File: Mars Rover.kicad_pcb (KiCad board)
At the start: 2 copper layers, 39 parts, among them U1401 PCA9685PW, U1402 ADS7828, U202 L298HN, U402 L298HN, U502 L298HN

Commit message: on to pcbs
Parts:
- added C101: 22uF, Capacitor_SMD:C_0805_2012Metric, F.Cu at (54.1, 139.1)
- added C102: 0.1uF, Capacitor_SMD:C_0805_2012Metric, F.Cu at (61.0, 137.3)
- added C1401: C, Capacitor_SMD:C_0805_2012Metric, F.Cu at (119.9, 21.3)
- added C201: 100nF, Capacitor_SMD:C_0805_2012Metric, F.Cu at (198.3, 53.4)
- added C202: 100nF, Capacitor_SMD:C_0805_2012Metric, F.Cu at (201.7, 53.4)
- added C203: 100nF, Capacitor_SMD:C_0805_2012Metric, F.Cu at (205.1, 53.4)
- added C401: 100nF, Capacitor_SMD:C_0805_2012Metric, F.Cu at (130.5, 118.3)
- added C402: 100nF, Capacitor_SMD:C_0805_2012Metric, F.Cu at (133.9, 118.3)
- added C403: 100nF, Capacitor_SMD:C_0805_2012Metric, F.Cu at (137.3, 118.3)
- added C501: 100nF, Capacitor_SMD:C_0805_2012Metric, F.Cu at (112.9, 127.2)
- added C502: 100nF, Capacitor_SMD:C_0805_2012Metric, F.Cu at (116.3, 127.2)
- added C503: 100nF, Capacitor_SMD:C_0805_2012Metric, F.Cu at (119.7, 127.2)
- added C601: 0.1uF, Capacitor_SMD:C_0805_2012Metric, F.Cu at (211.3, 25.3)
- added C602: 0.1uF, Capacitor_SMD:C_0805_2012Metric, F.Cu at (214.7, 23.3)
- added C603: 1nF, Capacitor_SMD:C_0805_2012Metric, F.Cu at (218.2, 21.3)
- added C604: 1uF, Capacitor_SMD:C_0805_2012Metric, F.Cu at (211.3, 27.2)
- added C605: 0.1uF, Capacitor_SMD:C_0805_2012Metric, F.Cu at (208.6, 31.2)
- added C606: 0.1uF, Capacitor_SMD:C_0805_2012Metric, F.Cu at (214.7, 27.2)
- added C607: 1nF, Capacitor_SMD:C_0805_2012Metric, F.Cu at (218.1, 23.2)
- added C608: 1nF, Capacitor_SMD:C_0805_2012Metric, F.Cu at (214.7, 25.3)
- added C609: C, Capacitor_SMD:C_0805_2012Metric, F.Cu at (211.3, 29.2)
- added C610: 0.1uF, Capacitor_SMD:C_0805_2012Metric, F.Cu at (207.9, 25.4)
- added C611: 0.1uF, Capacitor_SMD:C_0805_2012Metric, F.Cu at (201.8, 32.3)
- added C612: 0.1uF, Capacitor_SMD:C_0805_2012Metric, F.Cu at (211.3, 23.3)
- added C613: 0.22uF, Capacitor_SMD:C_0805_2012Metric, F.Cu at (214.8, 21.3)
- added C614: 22uF, Capacitor_SMD:C_0805_2012Metric, F.Cu at (207.9, 27.3)
- added C615: 4.7uF, Capacitor_SMD:C_0805_2012Metric, F.Cu at (205.2, 32.3)
- added C616: 22uF, Capacitor_SMD:C_0805_2012Metric, F.Cu at (207.9, 29.3)
- added C701: C, Capacitor_SMD:C_0805_2012Metric, F.Cu at (94.5, 160.7)
- added C702: C, Capacitor_SMD:C_0805_2012Metric, F.Cu at (87.6, 155.2)
- added C703: 220pF, Capacitor_SMD:C_0805_2012Metric, F.Cu at (87.2, 163.7)
- added C704: 220pF, Capacitor_SMD:C_0805_2012Metric, F.Cu at (77.2, 156.1)
- added C801: C, Capacitor_SMD:C_0805_2012Metric, F.Cu at (205.2, 44.0)
- added C802: C, Capacitor_SMD:C_0805_2012Metric, F.Cu at (201.8, 44.0)
- added C803: 220pF, Capacitor_SMD:C_0805_2012Metric, F.Cu at (205.8, 40.5)
- added C804: 220pF, Capacitor_SMD:C_0805_2012Metric, F.Cu at (209.2, 38.6)
- added D1001: DIODE, Diode_SMD:D_0805_2012Metric, F.Cu at (233.6, 23.4)
- added D1002: DIODE, Diode_SMD:D_0805_2012Metric, F.Cu at (226.7, 25.0)
- added D1003: DIODE, Diode_SMD:D_0805_2012Metric, F.Cu at (230.1, 25.0)
- added D1004: DIODE, Diode_SMD:D_0805_2012Metric, F.Cu at (232.9, 21.3)
- added D1101: DIODE, Diode_SMD:D_0805_2012Metric, F.Cu at (106.4, 127.9)
- added D1102: DIODE, Diode_SMD:D_0805_2012Metric, F.Cu at (103.0, 129.5)
- added D1103: DIODE, Diode_SMD:D_0805_2012Metric, F.Cu at (105.7, 125.9)
- added D1104: DIODE, Diode_SMD:D_0805_2012Metric, F.Cu at (99.5, 129.5)
- added D1201: DIODE, Diode_SMD:D_0805_2012Metric, F.Cu at (93.0, 136.8)
- added D1202: DIODE, Diode_SMD:D_0805_2012Metric, F.Cu at (89.5, 138.4)
- added D1203: DIODE, Diode_SMD:D_0805_2012Metric, F.Cu at (92.3, 134.7)
- added D1204: DIODE, Diode_SMD:D_0805_2012Metric, F.Cu at (86.1, 138.4)
- added D1301: DIODE, Diode_SMD:D_0805_2012Metric, F.Cu at (120.5, 118.3)
- added D1302: DIODE, Diode_SMD:D_0805_2012Metric, F.Cu at (123.3, 114.7)
- added D1303: DIODE, Diode_SMD:D_0805_2012Metric, F.Cu at (117.1, 118.3)
- added D1304: DIODE, Diode_SMD:D_0805_2012Metric, F.Cu at (124.0, 116.7)
- added D301: DIODE, Diode_SMD:D_0805_2012Metric, F.Cu at (107.1, 118.3)
- added D302: DIODE, Diode_SMD:D_0805_2012Metric, F.Cu at (110.5, 116.7)
- added D303: DIODE, Diode_SMD:D_0805_2012Metric, F.Cu at (109.8, 114.7)
- added D304: DIODE, Diode_SMD:D_0805_2012Metric, F.Cu at (103.6, 118.3)
- added D601: DIODE, Diode_SMD:D_0805_2012Metric, F.Cu at (198.3, 32.4)
- added D602: D_Schottky, Diode_SMD:D_0805_2012Metric, F.Cu at (207.9, 21.3)
- added D603: D_Schottky, Diode_SMD:D_0805_2012Metric, F.Cu at (211.3, 21.3)
- added D604: DIODE, Diode_SMD:D_0805_2012Metric, F.Cu at (207.9, 23.4)
- added D701: D_Schottky, Diode_SMD:D_0805_2012Metric, F.Cu at (83.1, 156.0)
- added D801: D_Schottky, Diode_SMD:D_0805_2012Metric, F.Cu at (198.3, 44.1)
- added D901: DIODE, Diode_SMD:D_0805_2012Metric, F.Cu at (93.0, 127.9)
- added D902: DIODE, Diode_SMD:D_0805_2012Metric, F.Cu at (89.5, 129.5)
- added D903: DIODE, Diode_SMD:D_0805_2012Metric, F.Cu at (92.3, 125.9)
- added D904: DIODE, Diode_SMD:D_0805_2012Metric, F.Cu at (86.1, 129.5)
- added H101: MountingHole_Pad, MountingHole:MountingHole_3.2mm_M3_Pad, F.Cu at (69.7, 132.8)
- added H102: MountingHole, MountingHole:MountingHole_3.2mm_M3, F.Cu at (69.7, 125.9)
- added H103: MountingHole, MountingHole:MountingHole_3.2mm_M3, F.Cu at (62.8, 132.8)
- added H104: MountingHole, MountingHole:MountingHole_3.2mm_M3, F.Cu at (75.8, 117.1)
- added H105: MountingHole, MountingHole:MountingHole_3.2mm_M3, F.Cu at (55.8, 134.6)
- added H106: MountingHole, MountingHole:MountingHole_3.2mm_M3, F.Cu at (62.8, 125.9)
- added J1: Barrel_Jack, Connector_BarrelJack:BarrelJack_CUI_PJ-102AH_Horizontal, F.Cu at (38.0, 115.5)
- added J101: Conn_01x02, Connector_PinHeader_2.54mm:PinHeader_1x02_P2.54mm_Vertical, F.Cu at (42.8, 135.2)
- added J102: Conn_01x03, Connector_PinHeader_2.54mm:PinHeader_1x03_P2.54mm_Vertical_SMD_Pin1Right, F.Cu at (61.9, 118.0)
- added J103: Conn_01x03, Connector_PinHeader_2.54mm:PinHeader_1x03_P2.54mm_Vertical_SMD_Pin1Right, F.Cu at (48.9, 126.8)
- added J104: Conn_01x03, Connector_PinHeader_2.54mm:PinHeader_1x03_P2.54mm_Vertical_SMD_Pin1Right, F.Cu at (55.0, 118.0)
- added J105: Conn_01x03, Connector_PinHeader_2.54mm:PinHeader_1x03_P2.54mm_Vertical_SMD_Pin1Right, F.Cu at (48.0, 118.0)
- added J106: Conn_01x03, Connector_PinHeader_2.54mm:PinHeader_1x03_P2.54mm_Vertical_SMD_Pin1Right, F.Cu at (68.9, 118.0)
- added J107: Conn_01x03, Connector_PinHeader_2.54mm:PinHeader_1x03_P2.54mm_Vertical_SMD_Pin1Right, F.Cu at (48.9, 135.5)
- added J108: Conn_01x03, Connector_PinHeader_2.54mm:PinHeader_1x03_P2.54mm_Vertical_SMD_Pin1Right, F.Cu at (55.8, 126.8)
- added J109: Conn_01x01, Connector_PinHeader_2.54mm:PinHeader_1x01_P2.54mm_Horizontal, F.Cu at (34.8, 131.5)
- added J1401: Raspberry_Pi_2_3, Roverschemlib:raspi3, F.Cu at (36.6, 47.2)
- added L601: INDUCTOR, Inductor_SMD:L_0805_2012Metric, F.Cu at (208.6, 33.2)
- added L701: L, Inductor_SMD:L_0805_2012Metric, F.Cu at (80.1, 157.0)
- added L801: L, Inductor_SMD:L_0805_2012Metric, F.Cu at (205.8, 38.6)
- added M1001: Motor_DC, Connector_PinHeader_2.54mm:PinHeader_2x01_P2.54mm_Vertical, F.Cu at (226.8, 22.1)
- added M1101: Motor_DC, Connector_PinHeader_2.54mm:PinHeader_2x01_P2.54mm_Vertical, F.Cu at (99.6, 126.7)
- added M1201: Motor_DC, Connector_PinHeader_2.54mm:PinHeader_2x01_P2.54mm_Vertical, F.Cu at (86.1, 135.5)
- added M1301: Motor_DC, Connector_PinHeader_2.54mm:PinHeader_2x01_P2.54mm_Vertical, F.Cu at (117.1, 115.5)
- added M301: Motor_DC, Connector_PinHeader_2.54mm:PinHeader_2x01_P2.54mm_Vertical, F.Cu at (103.7, 115.5)
- added M901: Motor_DC, Connector_PinHeader_2.54mm:PinHeader_2x01_P2.54mm_Vertical, F.Cu at (86.1, 126.7)
- added SW1: KILLSWITCH, Connector_PinHeader_2.54mm:PinHeader_1x02_P2.54mm_Vertical, F.Cu at (75.0, 122.4)
- added SW101: CHARGING, Connector_PinHeader_2.54mm:PinHeader_1x02_P2.54mm_Vertical, F.Cu at (78.7, 122.4)
- added U101: 74HCT244, Package_SO:TSSOP-20_4.4x6.5mm_P0.65mm, F.Cu at (37.0, 136.9)
- added U1403: Rpi0w, Roverschemlib:raspi0w, F.Cu at (36.6, 103.1)
- added U201: OP279, Package_SO:TSSOP-8_4.4x3mm_P0.65mm, F.Cu at (200.6, 50.6)
- added U401: OP279, Package_SO:TSSOP-8_4.4x3mm_P0.65mm, F.Cu at (132.7, 115.5)
- added U501: OP279, Package_SO:TSSOP-8_4.4x3mm_P0.65mm, F.Cu at (115.2, 124.4)
- added U601: MAX1758, Package_SO:SSOP-28_5.3x10.2mm_P0.65mm, F.Cu at (201.4, 25.8)
- added U701: MP2467, Package_SO:SOIC-8_3.9x4.9mm_P1.27mm, F.Cu at (87.7, 158.9)
- added U801: MP2467, Package_SO:SOIC-8_3.9x4.9mm_P1.27mm, F.Cu at (200.4, 40.3)
- moved R703 273.1 mm to (81.9, 162.8)
- moved R704 269.8 mm to (82.0, 160.8), turned to 180 degrees
- moved R702 266.1 mm to (89.2, 163.7), turned to 90 degrees
- moved R701 263.3 mm to (92.5, 160.6), turned to 90 degrees
- moved U1401 240.8 mm to (320.0, 158.8)
- moved R1404 225.7 mm to (318.9, 147.7)
- moved R201 225.7 mm to (281.1, 136.5)
- moved R203 225.7 mm to (287.9, 136.5)
- moved R206 225.7 mm to (298.2, 136.5)
- moved R401 225.7 mm to (281.1, 153.0)
- moved R403 225.7 mm to (287.9, 153.0)
- moved R406 225.7 mm to (298.2, 153.0)
- moved R501 225.7 mm to (308.2, 136.5)
- moved R503 225.7 mm to (315.0, 136.5)
- moved R603 225.7 mm to (335.2, 127.4)
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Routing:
- net Net-(C702-Pad2): track 0.00 -> 6.74 mm
- net +5V: track 0.00 -> 6.56 mm
- net Net-(C703-Pad1): track 0.00 -> 5.03 mm
- net /VMOTOR: track 0.00 -> 4.70 mm
- net Net-(R703-Pad2): track 0.00 -> 4.18 mm
- net Net-(C702-Pad1): track 0.00 -> 2.58 mm
- net Net-(R701-Pad2): track 0.00 -> 2.17 mm
- net Net-(C703-Pad2): track 0.00 -> 2.00 mm

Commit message: PCB - MAX 1758
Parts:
- moved L801 158.4 mm to (103.9, 159.8), turned to 90 degrees
- moved C803 158.0 mm to (105.9, 162.9), turned to 270 degrees
- moved C804 157.9 mm to (104.7, 157.0)
- moved U801 150.4 mm to (111.2, 161.4)
- moved D801 148.3 mm to (105.7, 159.8), turned to 90 degrees
- moved C801 148.2 mm to (115.8, 162.3), turned to 270 degrees
- moved C802 145.5 mm to (111.1, 157.7), turned to 180 degrees
- moved C503 106.0 mm to (192.8, 50.3), turned to 270 degrees
- moved D1201 49.8 mm to (141.7, 126.6)
- moved D1203 49.8 mm to (141.0, 124.6)
- moved D1204 49.8 mm to (134.8, 128.2)
- moved M1201 49.8 mm to (134.9, 125.4)
- moved D1202 47.8 mm to (136.1, 128.0)
- moved U501 30.1 mm to (142.2, 137.6)
- moved C607 29.2 mm to (189.0, 25.4), turned to 180 degrees
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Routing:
- net Net-(C609-Pad1): track 0.00 -> 11.8 mm
- net /VMOTOR: track 4.70 -> 15.9 mm
- net Net-(C609-Pad2): track 0.00 -> 10.2 mm
- net /Battery Connection and Charge Management/CHRG_VL: track 0.00 -> 9.92 mm
- net Net-(C802-Pad2): track 0.00 -> 7.84 mm
- net Net-(C602-Pad2): track 0.00 -> 7.25 mm
- net Net-(C604-Pad2): track 0.00 -> 7.24 mm
- net Net-(C611-Pad2): track 0.00 -> 6.81 mm
- net Net-(C612-Pad1): track 0.00 -> 5.69 mm
- net Net-(C608-Pad1): track 0.00 -> 4.21 mm
- net Net-(C606-Pad1): track 0.00 -> 3.03 mm
- net Net-(C603-Pad1): track 0.00 -> 2.76 mm
- net +12V: track 0.00 -> 2.59 mm
- net Net-(C802-Pad1): track 0.00 -> 2.58 mm
- net Net-(C803-Pad1): track 0.00 -> 2.58 mm
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
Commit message: More layout
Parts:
- moved U1401 296.8 mm to (24.2, 135.4)
- moved R803 256.6 mm to (80.0, 176.2)
- moved R804 256.1 mm to (79.9, 174.2), turned to 180 degrees
- moved R802 246.0 mm to (87.0, 176.7), turned to 90 degrees
- moved R801 242.3 mm to (90.7, 173.6), turned to 90 degrees
- moved R602 235.1 mm to (103.6, 129.7)
- moved R603 231.7 mm to (103.6, 127.7)
- moved R604 218.4 mm to (116.9, 120.8), turned to 180 degrees
- moved R601 214.5 mm to (124.1, 127.8)
- moved R1402 208.1 mm to (116.9, 116.6), turned to 180 degrees
- moved R1404 204.1 mm to (116.9, 118.7), turned to 180 degrees
- moved R1403 196.0 mm to (121.8, 119.7), turned to 90 degrees
- moved R1401 193.6 mm to (123.9, 119.7), turned to 270 degrees
- moved U1402 181.5 mm to (140.7, 104.2), turned to 180 degrees
- moved R405 143.6 mm to (191.5, 53.2), turned to 90 degrees
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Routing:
- net /sheet5C45DA5C/V2: track 0.00 -> 21.6 mm
- net /sheet5C45DEF9/V1: track 0.00 -> 20.7 mm
- net /sheet5C45F77A/V2: track 0.00 -> 20.6 mm
- net /sheet5C45D717/V1: track 0.00 -> 20.5 mm
- net /Motor/V2: track 0.00 -> 20.3 mm
- net /sheet5C45FA3C/V1: track 0.00 -> 20.1 mm
- net Net-(R405-Pad1): track 0.00 -> 16.3 mm
- net Net-(R505-Pad1): track 0.00 -> 16.3 mm
- net Net-(R406-Pad1): track 0.00 -> 16.2 mm
- net Net-(R206-Pad1): track 0.00 -> 15.7 mm
- net /sheet5C45FA3C/V2: track 0.00 -> 15.5 mm
- net /sheet5C45DEF9/V2: track 0.00 -> 15.4 mm
- net /sheet5C45DA5C/V1: track 0.00 -> 15.4 mm
- net /sheet5C45D717/V2: track 0.00 -> 15.2 mm
- net /sheet5C45F77A/V1: track 0.00 -> 14.9 mm
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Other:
- board text added: "Move diodes away, populate screw terminal blocks"

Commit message: updated layout
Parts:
- removed U1403: Rpi0w, Roverschemlib:raspi0w
- added J1402: Conn_01x02, Connector_PinSocket_2.54mm:PinSocket_1x02_P2.54mm_Vertical, F.Cu at (-102.0, 135.0)
- J102, J103, J104, J105, J106, J107, J108: footprint Connector_PinHeader_2.54mm:PinHeader_1x03_P2.54mm_Vertical_SMD_Pin1Right -> Connector_PinHeader_2.54mm:PinHeader_1x03_P2.54mm_Vertical
- J1401: footprint Roverschemlib:raspi3 -> Connector_PinSocket_2.54mm:PinSocket_2x20_P2.54mm_Vertical
- moved SW1 230.0 mm to (-154.2, 104.2), turned to 180 degrees
- moved H104 220.7 mm to (-141.0, 158.4)
- moved H101 220.6 mm to (-149.5, 157.4)
- moved H102 220.6 mm to (-149.5, 150.5)
- moved H103 220.6 mm to (-156.4, 157.4)
- moved H106 220.6 mm to (-156.4, 150.5)
- moved C201 205.2 mm to (-47.3, 146.9)
- moved C203 205.2 mm to (-38.1, 146.4)
- moved C403 205.2 mm to (-45.1, 140.7)
- moved C501 205.2 mm to (-33.5, 146.4)
- moved C503 205.2 mm to (-42.7, 146.4)
- moved C1401 199.1 mm to (-40.0, 140.0)
- moved H105 197.3 mm to (-140.8, 150.5)
- moved J1 192.3 mm to (-154.2, 110.5)
- moved SW101 173.5 mm to (-94.4, 134.7)
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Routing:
- net /Digital logic/SCL: track 0.00 -> 33.2 mm
- net GND: track 3.44 -> 34.6 mm, vias 1 -> 9
- net Net-(R1402-Pad1): track 2.08 -> 32.8 mm
- net Net-(J104-Pad2): track 0.00 -> 28.5 mm
- net /Battery Connection and Charge Management/~FAULT: track 0.00 -> 26.7 mm
- net Net-(J102-Pad2): track 0.00 -> 26.3 mm
- net Net-(J105-Pad2): track 0.00 -> 26.2 mm
- net Net-(R1401-Pad1): track 2.09 -> 28.3 mm
- net /Digital logic/SDA: track 0.00 -> 25.4 mm
- net /Battery Connection and Charge Management/CHRG_VL: track 9.92 -> 32.0 mm
- net /Digital logic/~OE: track 0.00 -> 20.5 mm
- net /Battery Connection and Charge Management/~FULLCHRG: track 0.00 -> 19.3 mm, vias 0 -> 1
- net /Battery Connection and Charge Management/~FASTCHRG: track 0.00 -> 19.2 mm, vias 0 -> 1
- net /Digital logic/PWM6: track 0.00 -> 18.4 mm
- net Net-(J1401-Pad7): track 0.00 -> 16.9 mm
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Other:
- board outline added: 150 x 100 mm
- board text added: "ARES - Mars Rover ICSS Electronics H.E., M.N., S.G."
- board text added: "Do Welsh androids cream to electric sheep?"
- board text added: "If found return to space"
- board text added: "Ranul is jacked as fuuuck"

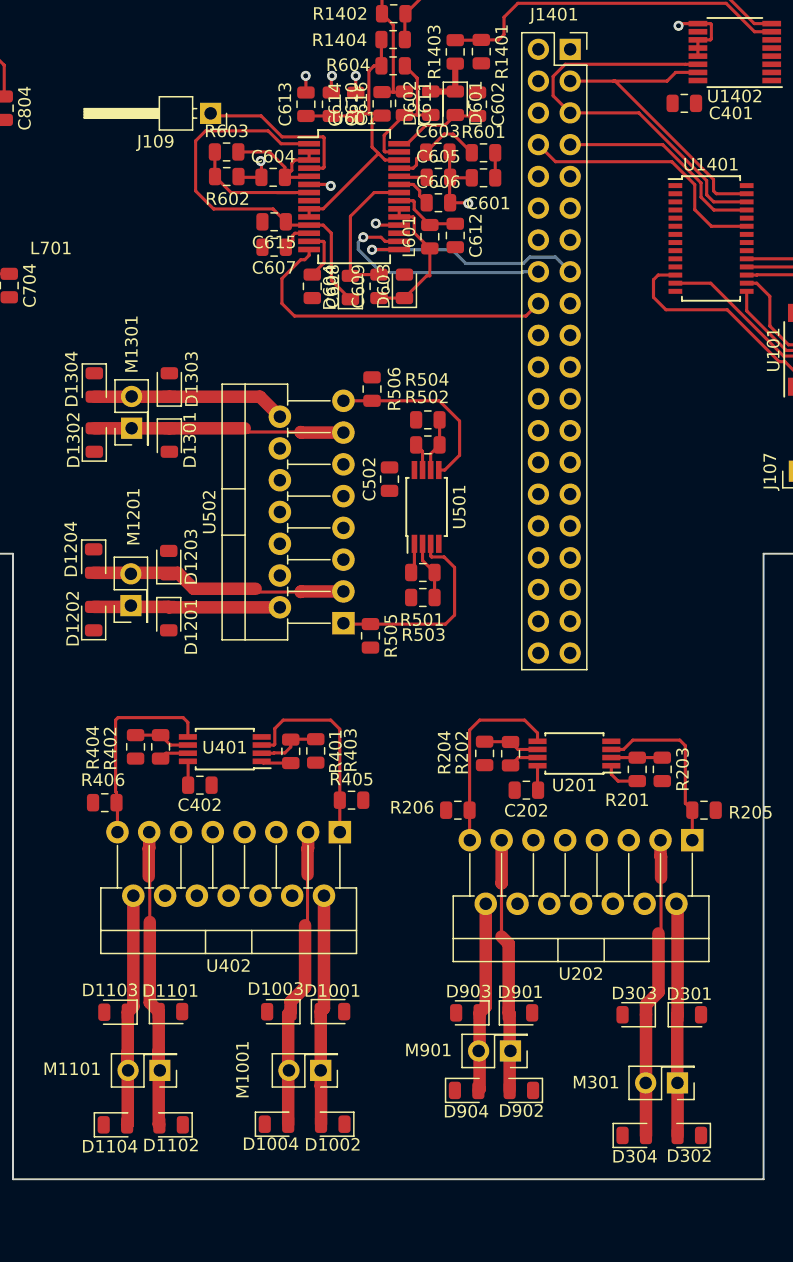
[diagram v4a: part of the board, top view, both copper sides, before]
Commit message: Fixed Courtyard violations and moved diodes away from motor screw terminals
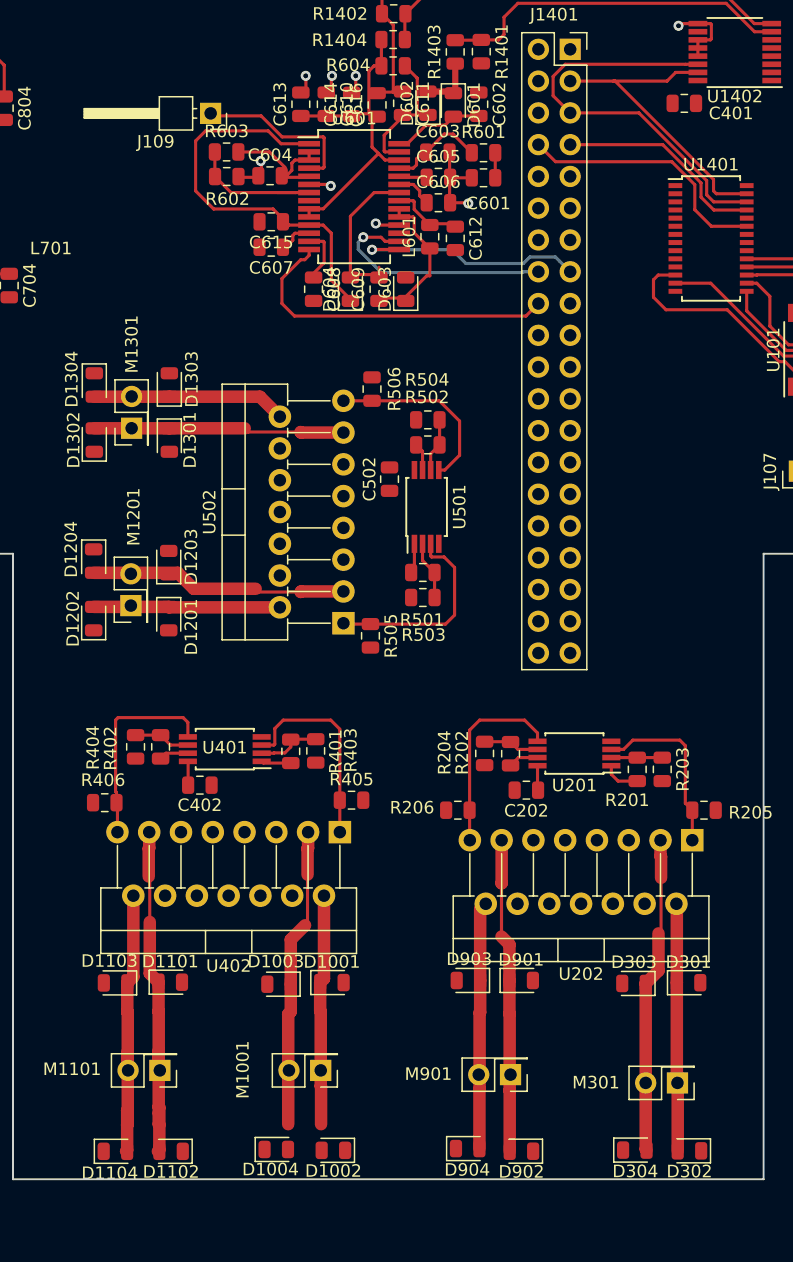
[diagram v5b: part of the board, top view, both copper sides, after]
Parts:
- moved D902 4.86 mm to (135.7, 150.4)
- moved D904 4.65 mm to (131.4, 150.2)
- moved D901 2.59 mm to (135.7, 136.7)
- moved D903 2.59 mm to (131.5, 136.7)
- moved D301 2.56 mm to (149.1, 136.9)
- moved D303 2.50 mm to (144.7, 136.9)
- moved D1101 2.35 mm to (107.7, 136.8)
- moved D1103 2.34 mm to (103.3, 136.9)
- moved D1001 2.32 mm to (120.6, 136.9)
- moved D1003 2.20 mm to (116.4, 137.0)
- moved D1102 2.12 mm to (107.7, 150.4)
- moved D1104 2.12 mm to (103.3, 150.4)
- moved D1002 2.09 mm to (120.7, 150.3)
- moved D1004 2.02 mm to (116.1, 150.2)
- moved M901 1.90 mm to (134.9, 144.2)
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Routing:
- net /sheet5C45DEF9/V1: track 25.4 -> 32.1 mm
- net /sheet5C45D717/V1: track 20.5 -> 25.3 mm
- net /sheet5C45D717/V2: track 15.2 -> 19.8 mm
- net /sheet5C45DEF9/V2: track 20.1 -> 23.5 mm
- net /Motor/V1: track 18.6 -> 20.0 mm
- net /Motor/V2: track 24.1 -> 25.3 mm
